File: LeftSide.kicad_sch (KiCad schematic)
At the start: 28 parts, among them J1 USB_C_Receptacle_USB2.0_14P, J2 Conn_01x02, U1 RP2040, U3 AP2112K-3.3, U4 W25Q128JVS, Y1 12MHz Crystal GND24

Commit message: Added USBC interconnect
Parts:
- removed C1, C2: 1u, symbol Device:C
- removed J1: USB_C_Receptacle_USB2.0_14P, symbol Connector:USB_C_Receptacle_USB2.0_14P
- removed R3: 5.1k, symbol Device:R
- removed R4: 5.1K, symbol Device:R
- removed U3: AP2112K-3.3, Package_TO_SOT_SMD:SOT-23-5, symbol Regulator_Linear:AP2112K-3.3
- added J7: USB_C_Receptacle_USB2.0_14P, symbol Connector:USB_C_Receptacle_USB2.0_14P
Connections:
- net +3V3: now also J7.A4 (VBUS), J7.A9 (VBUS), J7.B4 (VBUS), J7.B9 (VBUS)
- net GND: now also J7.A1 (GND), J7.A12 (GND), J7.B1 (GND), J7.B12 (GND), J7.S1 (SHIELD)
- net GPIO_1: now reaches U1.3 (GPIO1)
- net GPIO_1: now also J7.A7 (D-), J7.B7 (D-)
- net GPIO_2: now reaches U1.4 (GPIO2)
- net GPIO_2: now also J7.A6 (D+), J7.B6 (D+)
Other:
- note added: "USBC Interconnect"
- note removed: "USBC Receptacle, LDO 5V -3.3V"
- moved on the sheet: C15, C16, R6, Y1

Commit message: Added Footprints
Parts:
- removed J2: Conn_01x02, symbol Connector_Generic:Conn_01x02
- added SW2: SW_Push, Button_Switch_SMD:Nidec_Copal_CAS-120A, symbol Switch:SW_Push
- added SW3: SW_Push, Package_SO:SOIC-8_3.9x4.9mm_P1.27mm, symbol Switch:SW_Push
- C10, C11, C12, C13, C14, C15, C16, C3, C4, C5, C6, C7, C8, C9: footprint (none) -> Capacitor_SMD:C_0603_1608Metric_Pad1.08x0.95mm_HandSolder
- R1, R2, R5, R6: footprint (none) -> Resistor_SMD:R_0201_0603Metric_Pad0.64x0.40mm_HandSolder
- Y1: footprint (none) -> Crystal:Crystal_SMD_3225-4Pin_3.2x2.5mm
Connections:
- net +3.3V: now also U1.56 (QSPI_SS)
- net GND: now also U1.19 (TESTEN), U1.57 (GND), SW2.1, SW3.1
- net RUN: now also SW2.2
- net at R5.1: now also SW3.2
- net QSPI_SD3: now reaches U1.51 (QSPI_SD3)
- net QSPI_SD3: now also U4.7 (~{HOLD}/~{RESET}/IO_{3})
- net QSPI_SCLK: now reaches U1.52 (QSPI_SCLK)
- net QSPI_SCLK: now also U4.6 (CLK)
- net QSPI_SDO: now reaches U1.53 (QSPI_SD0)
- net QSPI_SDO: now also U4.5 (DI/IO_{0})
- net QSPI_SD2: now reaches U1.54 (QSPI_SD2)
- net QSPI_SD2: now also U4.3 (~{WP}/IO_{2})
- net QSPI_SD1: now reaches U1.55 (QSPI_SD1)
- net QSPI_SD1: now also U4.2 (DO/IO_{1})

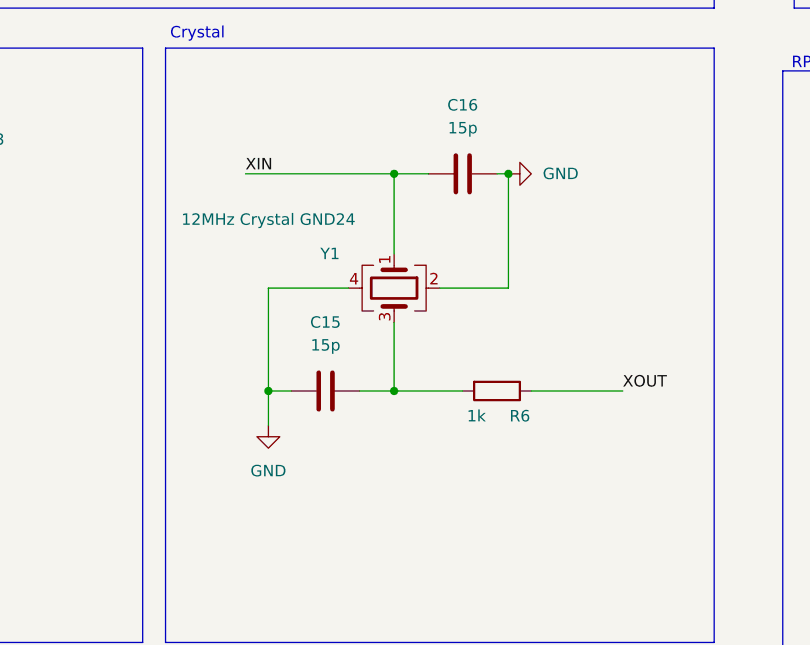
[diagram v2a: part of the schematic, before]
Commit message: Added footprints and started PCB layout
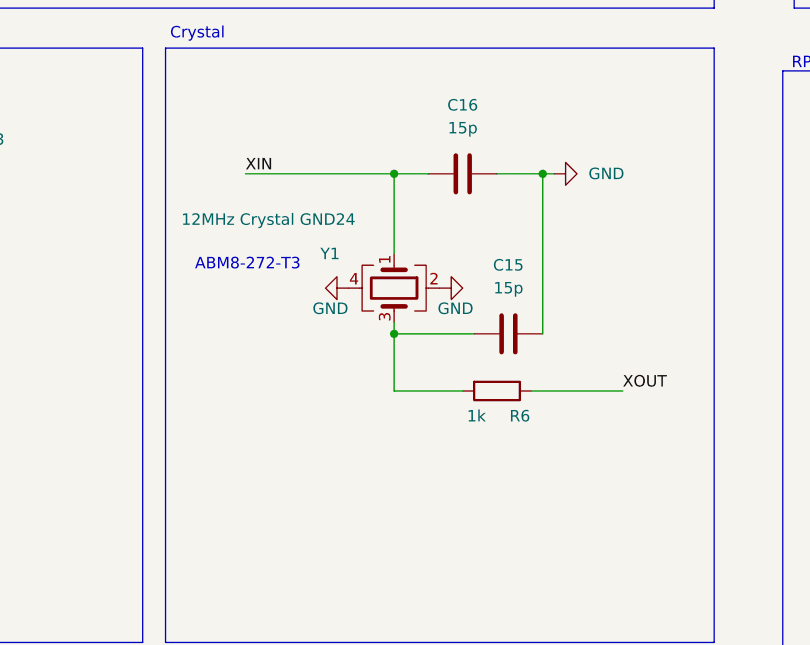
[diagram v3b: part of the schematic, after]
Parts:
- J7: footprint (none) -> Connector_USB:USB_C_Receptacle_GCT_USB4125-xx-x-0190_6P_TopMnt_Horizontal
- SW2: footprint Button_Switch_SMD:Nidec_Copal_CAS-120A -> PTS636_SM43J_SMTR_LFS:SW_PTS636_SM43J_SMTR_LFS
- SW3: footprint Package_SO:SOIC-8_3.9x4.9mm_P1.27mm -> PTS636_SM43J_SMTR_LFS:SW_PTS636_SM43J_SMTR_LFS
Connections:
- net GND: now also C15.2; no longer C15.1
- net at R6.2, Y1.3: now also C15.1; no longer C15.2
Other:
- note added: "ABM8-272-T3"
- moved on the sheet: C15
